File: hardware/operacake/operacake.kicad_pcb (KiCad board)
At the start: 4 copper layers, 120 x 75 mm, 152 parts, among them J1 CONN_02X20, J2 CONN_02X20, P1 ADDRESS, P20 GPIO, P22 I2S, P28 SD, P9 BASEBAND, U1 MASWSS0129, U10 74LVC1G58, U11 74LVC1G58, U12 74LVC1G58, U13 74LVC1G58, U14 74AHC1G02, U15 74AHC1G02, U16 74LVC1G19, U2 SKY13322, U3 SKY13322, U4 PCA9557, U5 TC7MBL3245CFT, U6 74LVC1G58, U7 74LVC1G58, U8 74AHC1G08, U9 74AHC1G08

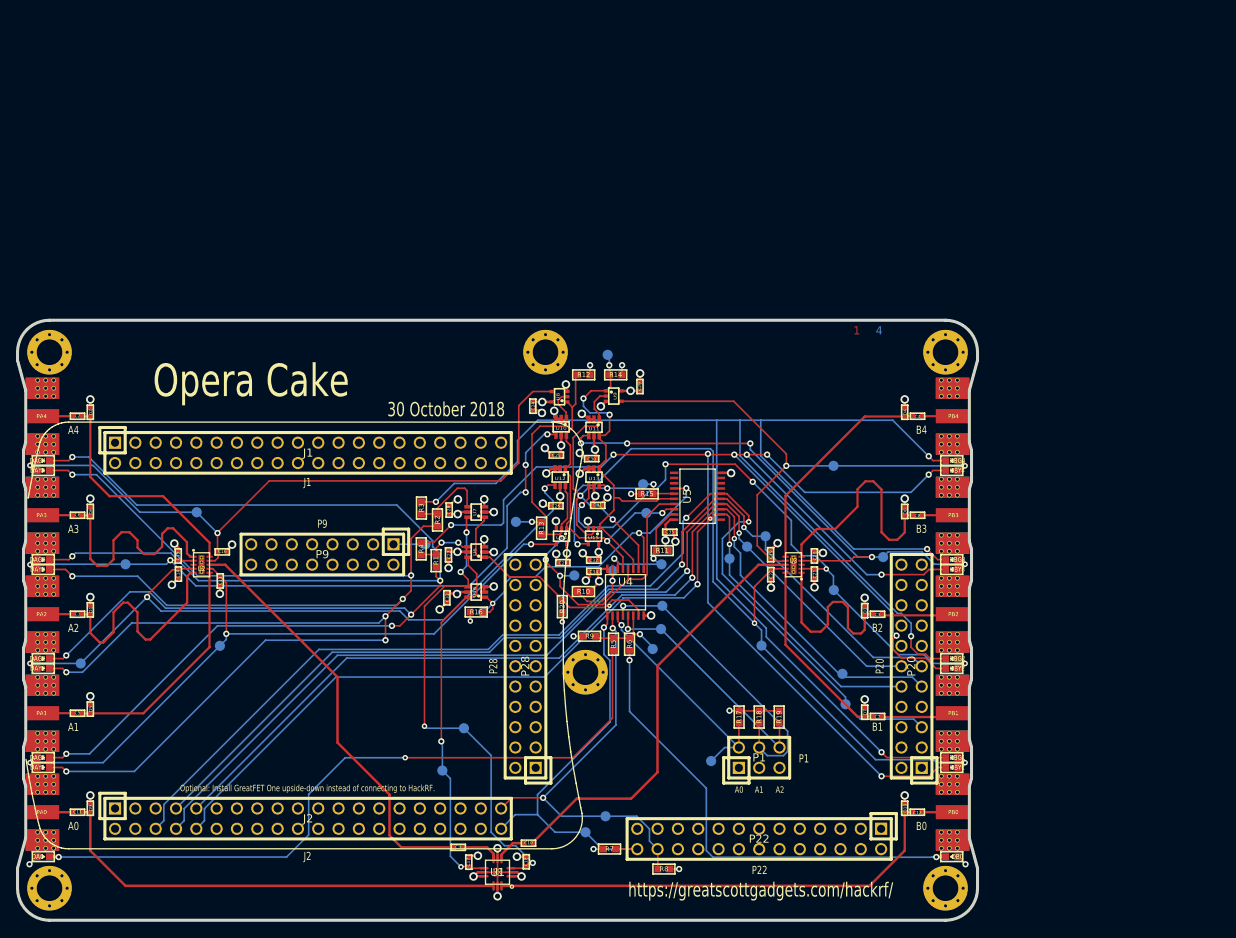
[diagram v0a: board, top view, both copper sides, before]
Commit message: OC Hardware: Update kicad files for KiCAD 7
	Add KiCAD 7 files
	Add VERSION & DATE fields to accordance to GSG best practices
	Update other 'page settings' data
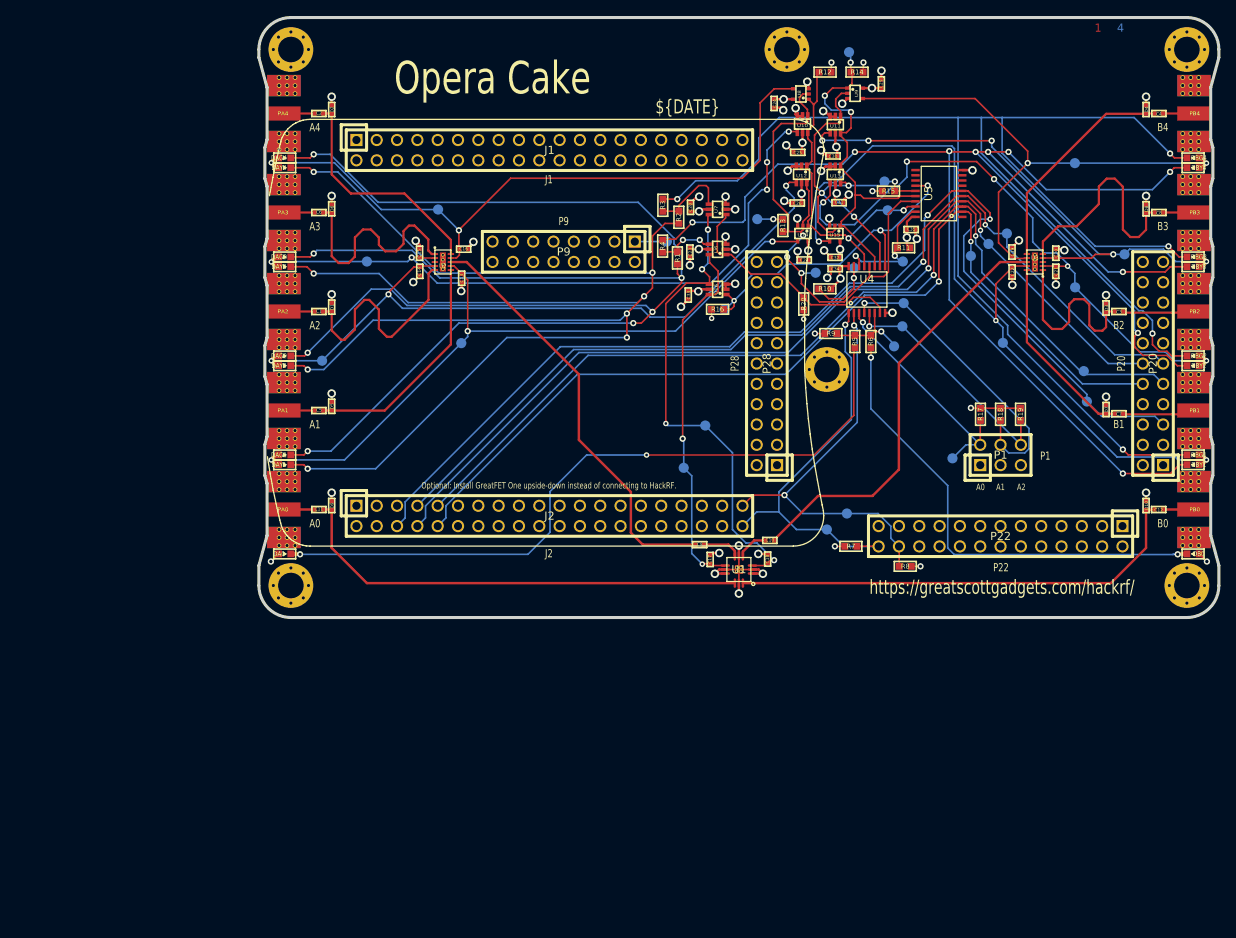
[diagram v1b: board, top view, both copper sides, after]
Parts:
- moved C33 48.4 mm to (143.8, 96.9)
- moved R20 48.4 mm to (158.3, 98.0)
- moved TP3 48.4 mm to (181.4, 90.5)
- moved C12 48.4 mm to (202.6, 123.7)
- moved C16 48.4 mm to (115.8, 91.1)
- moved C17 48.4 mm to (146.6, 129.9)
- moved C21 48.4 mm to (189.8, 93.9)
- moved C23 48.4 mm to (144.0, 91.5)
- moved C9 48.4 mm to (145.3, 128.0)
- moved DAG1 48.4 mm to (93.4, 116.8)
- moved DAG2 48.4 mm to (93.4, 104.5)
- moved DAG3 48.4 mm to (93.4, 92.1)
- moved J2 48.4 mm to (126.5, 124.5)
- moved P20 48.4 mm to (201.9, 105.4)
- moved P9 48.4 mm to (128.3, 91.4)
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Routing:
- added copper zone on In1.Cu, net GND
- added copper zone on In2.Cu, net VCC
- removed copper zone on C2, net GND
- removed copper zone on C3, net VCC
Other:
- net class Default removed
- board text added: "${ISSUE_DATE}"
- board text removed: "30 October 2018"
